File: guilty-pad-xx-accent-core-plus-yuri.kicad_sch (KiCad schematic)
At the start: 279 parts, among them J1 Conn_01x04_Socket, Q1 DMC3071LVT, SW1 SW_Push, SW10 SW_Push, SW11 SW_Push, SW12 SW_Push, SW13 SW_Push, SW14 SW_Push, SW15 SW_Push, SW16 SW_Push, SW17 SW_Push, SW18 SW_Push, SW19 SW_Push, SW2 SW_Push, SW20 SW_Push, SW21 SW_Push, SW22 SW_Push, SW23 SW_Push, SW24 SW_Push, SW25 SW_Push, SW26 SW_Push, SW27 SW_Push, SW28 SW_Push, SW29 SW_Push, SW3 SW_Push, SW30 SW_Push, SW31 SW_Push, SW32 SW_Push, SW33 SW_Push, SW34 SW_Push, SW35 SW_Push, SW36 SW_Push, SW37 SW_Push, SW38 SW_Push, SW39 SW_Push, SW4 SW_Push, SW40 SW_Push, SW41 SW_Push, SW42 SW_Push, SW43 SW_Push, SW44 SW_Push, SW45 SW_Push, SW46 SW_Push, SW47 SW_Push, SW48 SW_Push, SW49 SW_Push, SW5 SW_Push, SW50 SW_Push, SW51 SW_Push, SW52 SW_Push, SW53 SW_Push, SW54 SW_Push, SW55 SW_Push, SW56 SW_Push, SW57 SW_Push, SW58 SW_Push, SW59 SW_Push, SW6 SW_Push, SW60 SW_Push, SW61 SW_Push, SW62 SW_Push, SW63 SW_Push, SW64 SW_Push, SW65 SW_Push, SW66 SW_Push, SW67 SW_Push, SW68 SW_Push, SW69 SW_Push, SW7 SW_Push, SW70 SW_Push, SW71 SW_Push, SW72 SW_Push, SW73 SW_Push, SW74 SW_Push, SW75 SW_Push, SW76 SW_Push, SW77 SW_Push, SW78 SW_Push, SW79 SW_Push, SW8 SW_Push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

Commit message: schematic and pcb are done, images for those are added
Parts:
- removed LED88, LED89: MX_SK6803MINI-E, PCM_marbastlib-mx:LED_MX_6028R, symbol ggxxacpy:MX_SK6803MINI-E
- removed Q1: DMC3071LVT, Package_TO_SOT_SMD:TSOT-23-6_HandSoldering, symbol Transistor_FET:DMC3071LVT
- added Q1: G1NP02ELL, Package_TO_SOT_SMD:TSOT-23-6_HandSoldering, symbol ggxxacpy:G1NP02ELL
- added SW88: RotaryEncoder_Switch, Rotary_Encoder:RotaryEncoder_Alps_EC11E-Switch_Vertical_H20mm, symbol Device:RotaryEncoder_Switch
- D1, D10, D11, D12, D13, D14, D15, D16, D17, D18, D19, D2, D20, D21, D22, D23, D24, D25, D26, D27, D28, D29, D3, D30, D31, D32, D33, D34, D35, D36, D37, D38, D39, D4, D40, D41, D42, D43, D44, D45, D46, D47, D48, D49, D5, D50, D51, D52, D53, D54, D55, D56, D57, D58, D59, D6, D60, D61, D62, D63, D64, D65, D66, D67, D68, D69, D7, D70, D71, D72, D73, D74, D75, D76, D77, D78, D79, D8, D80, D81, D82, D83, D84, D85, D86, D87, D88, D9: footprint (none) -> Diode_SMD:D_SMA_Handsoldering
- D89: footprint Diode_SMD:D_SOD-123 -> Diode_SMD:D_SMA_Handsoldering
- J1: footprint (none) -> KiCad-SSD1306-0.91-OLED-4pin-128x32:SSD1306-0.91-OLED-4pin-128x32
- LED1, LED10, LED11, LED12, LED13, LED14, LED15, LED16, LED17, LED18, LED19, LED2, LED20, LED21, LED22, LED23, LED24, LED25, LED26, LED27, LED28, LED29, LED3, LED30, LED31, LED32, LED33, LED34, LED35, LED36, LED37, LED38, LED39, LED4, LED40, LED41, LED42, LED43, LED44, LED45, LED46, LED47, LED48, LED49, LED5, LED50, LED51, LED52, LED53, LED54, LED55, LED56, LED57, LED58, LED59, LED6, LED60, LED61, LED62, LED63, LED64, LED65, LED66, LED67, LED68, LED69, LED7, LED70, LED71, LED72, LED73, LED74, LED75, LED76, LED77, LED78, LED79, LED8, LED80, LED81, LED82, LED83, LED84, LED85, LED86, LED87, LED9: footprint PCM_marbastlib-mx:LED_MX_6028R -> gpxxacpy:LED_6028R
- R3, R4: footprint (none) -> Capacitor_SMD:C_0402_1005Metric_Pad0.74x0.62mm_HandSolder
- SW1, SW10, SW11, SW12, SW13, SW14, SW15, SW16, SW17, SW18, SW19, SW2, SW20, SW21, SW22, SW23, SW24, SW25, SW26, SW27, SW28, SW3, SW30, SW31, SW32, SW33, SW35, SW36, SW37, SW38, SW39, SW4, SW40, SW41, SW42, SW43, SW44, SW45, SW46, SW48, SW49, SW5, SW50, SW52, SW53, SW54, SW55, SW56, SW57, SW58, SW59, SW6, SW60, SW61, SW62, SW65, SW66, SW67, SW68, SW69, SW7, SW70, SW71, SW72, SW73, SW74, SW76, SW8, SW85, SW86, SW87, SW9: footprint (none) -> gpxxacpy:SW_Cherry_MX_1.00u_PCB
- SW29: footprint (none) -> gpxxacpy:SW_Cherry_MX_2.00u_PCB
- SW34, SW47: footprint (none) -> gpxxacpy:SW_Cherry_MX_1.50u_PCB
- SW51: footprint (none) -> gpxxacpy:SW_Cherry_MX_1.75u_PCB
- SW63, SW64: footprint (none) -> gpxxacpy:SW_Cherry_MX_2.25u_PCB
- SW75: footprint (none) -> gpxxacpy:SW_Cherry_MX_2.75u_PCB
- SW77, SW78, SW79, SW81, SW82, SW83, SW84: footprint (none) -> gpxxacpy:SW_Cherry_MX_1.25u_PCB
- SW80: footprint (none) -> gpxxacpy:SW_Cherry_MX_6.25u_PCB
- U1: footprint (none) -> OPL:XIAO-nRF52840-SMD
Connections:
- net +5V_USB: now also Q1.1 (G)
- net COL1: now also SW73.1, SW74.1, SW75.1, SW76.1, SW77.1, SW78.1, SW79.1, SW80.1, SW81.1
- net GND: now also Q1.5 (S), SW88.C, SW88.S2; no longer LED1.4 (VSS), LED10.4 (VSS), LED11.4 (VSS), LED12.4 (VSS), LED13.4 (VSS), LED14.4 (VSS), LED15.4 (VSS), LED16.4 (VSS), LED17.4 (VSS), LED18.4 (VSS), LED19.4 (VSS), LED2.4 (VSS), LED20.4 (VSS), LED21.4 (VSS), LED22.4 (VSS), LED23.4 (VSS), LED24.4 (VSS), LED25.4 (VSS), LED26.4 (VSS), LED27.4 (VSS), LED28.4 (VSS), LED29.4 (VSS), LED3.4 (VSS), LED30.4 (VSS), LED31.4 (VSS), LED32.4 (VSS), LED33.4 (VSS), LED34.4 (VSS), LED35.4 (VSS), LED36.4 (VSS), LED37.4 (VSS), LED38.4 (VSS), LED39.4 (VSS), LED4.4 (VSS), LED40.4 (VSS), LED41.4 (VSS), LED42.4 (VSS), LED43.4 (VSS), LED44.4 (VSS), LED45.4 (VSS), LED46.4 (VSS), LED47.4 (VSS), LED48.4 (VSS), LED49.4 (VSS), LED5.4 (VSS), LED50.4 (VSS), LED51.4 (VSS), LED52.4 (VSS), LED53.4 (VSS), LED54.4 (VSS), LED55.4 (VSS), LED56.4 (VSS), LED57.4 (VSS), LED58.4 (VSS), LED59.4 (VSS), LED6.4 (VSS), LED60.4 (VSS), LED61.4 (VSS), LED62.4 (VSS), LED63.4 (VSS), LED64.4 (VSS), LED65.4 (VSS), LED66.4 (VSS), LED67.4 (VSS), LED68.4 (VSS), LED69.4 (VSS), LED7.4 (VSS), LED70.4 (VSS), LED71.4 (VSS), LED72.4 (VSS), LED73.4 (VSS), LED74.4 (VSS), LED75.4 (VSS), LED76.4 (VSS), LED77.4 (VSS), LED78.4 (VSS), LED79.4 (VSS), LED8.4 (VSS), LED80.4 (VSS), LED81.4 (VSS), LED82.4 (VSS), LED83.4 (VSS), LED84.4 (VSS), LED85.4 (VSS), LED86.4 (VSS), LED87.4 (VSS), LED9.4 (VSS)
- net LED_ENABLE: now also Q1.3 (G)
- net LED_GND: now also LED1.4 (VSS), LED10.4 (VSS), LED11.4 (VSS), LED12.4 (VSS), LED13.4 (VSS), LED14.4 (VSS), LED15.4 (VSS), LED16.4 (VSS), LED17.4 (VSS), LED18.4 (VSS), LED19.4 (VSS), LED2.4 (VSS), LED20.4 (VSS), LED21.4 (VSS), LED22.4 (VSS), LED23.4 (VSS), LED24.4 (VSS), LED25.4 (VSS), LED26.4 (VSS), LED27.4 (VSS), LED28.4 (VSS), LED29.4 (VSS), LED3.4 (VSS), LED30.4 (VSS), LED31.4 (VSS), LED32.4 (VSS), LED33.4 (VSS), LED34.4 (VSS), LED35.4 (VSS), LED36.4 (VSS), LED37.4 (VSS), LED38.4 (VSS), LED39.4 (VSS), LED4.4 (VSS), LED40.4 (VSS), LED41.4 (VSS), LED42.4 (VSS), LED43.4 (VSS), LED44.4 (VSS), LED45.4 (VSS), LED46.4 (VSS), LED47.4 (VSS), LED48.4 (VSS), LED49.4 (VSS), LED5.4 (VSS), LED50.4 (VSS), LED51.4 (VSS), LED52.4 (VSS), LED53.4 (VSS), LED54.4 (VSS), LED55.4 (VSS), LED56.4 (VSS), LED57.4 (VSS), LED58.4 (VSS), LED59.4 (VSS), LED6.4 (VSS), LED60.4 (VSS), LED61.4 (VSS), LED62.4 (VSS), LED63.4 (VSS), LED64.4 (VSS), LED65.4 (VSS), LED66.4 (VSS), LED67.4 (VSS), LED68.4 (VSS), LED69.4 (VSS), LED7.4 (VSS), LED70.4 (VSS), LED71.4 (VSS), LED72.4 (VSS), LED73.4 (VSS), LED74.4 (VSS), LED75.4 (VSS), LED76.4 (VSS), LED77.4 (VSS), LED78.4 (VSS), LED79.4 (VSS), LED8.4 (VSS), LED80.4 (VSS), LED81.4 (VSS), LED82.4 (VSS), LED83.4 (VSS), LED84.4 (VSS), LED85.4 (VSS), LED86.4 (VSS), LED87.4 (VSS), LED9.4 (VSS), Q1.2 (S), Q1.4 (D)
- net ROW0: now also D18.1 (K), D35.1 (K), D52.1 (K), D78.1 (K); no longer D11.1 (K), D29.1 (K), D47.1 (K), D74.1 (K), D83.1 (K)
- net ROW1: now also D19.1 (K), D36.1 (K), D53.1 (K), D79.1 (K); no longer D12.1 (K), D30.1 (K), D48.1 (K), D75.1 (K), D84.1 (K)
- net ROW2: now also D17.1 (K), D29.1 (K), D45.1 (K), D48.1 (K), D62.1 (K), D73.1 (K), D74.1 (K), D84.1 (K); no longer D13.1 (K), D31.1 (K), D40.1 (K), D49.1 (K), D58.1 (K), D67.1 (K), D76.1 (K), D85.1 (K)
- net ROW3: now also D16.1 (K), D31.1 (K), D46.1 (K), D47.1 (K), D63.1 (K), D72.1 (K), D75.1 (K), D85.1 (K); no longer D14.1 (K), D32.1 (K), D41.1 (K), D50.1 (K), D59.1 (K), D68.1 (K), D77.1 (K), D86.1 (K)
- net ROW4: now also D30.1 (K), D44.1 (K), D54.1 (K), D64.1 (K), D67.1 (K), D77.1 (K), D88.1 (K); no longer D33.1 (K), D42.1 (K), D51.1 (K), D60.1 (K), D69.1 (K), D78.1 (K), D87.1 (K)
- net ROW5: now also D14.1 (K), D42.1 (K), D51.1 (K), D58.1 (K), D68.1 (K), D80.1 (K), D87.1 (K); no longer D16.1 (K), D43.1 (K), D52.1 (K), D61.1 (K), D70.1 (K), D79.1 (K), D88.1 (K)
- net ROW6: now also D13.1 (K), D33.1 (K), D43.1 (K), D50.1 (K), D59.1 (K), D69.1 (K), D81.1 (K), D86.1 (K); no longer D17.1 (K), D35.1 (K), D44.1 (K), D53.1 (K), D62.1 (K), D71.1 (K), D80.1 (K)
- net ROW7: now also D12.1 (K), D32.1 (K), D40.1 (K), D49.1 (K), D60.1 (K), D70.1 (K), D82.1 (K), D83.1 (K); no longer D18.1 (K), D36.1 (K), D45.1 (K), D54.1 (K), D63.1 (K), D72.1 (K), D81.1 (K)
- net ROW8: now also D11.1 (K), D41.1 (K), D61.1 (K), D71.1 (K), D76.1 (K); no longer D19.1 (K), D46.1 (K), D64.1 (K), D73.1 (K), D82.1 (K)
- net EC11_SW: now reaches U1.2 (P0.03_A1_D1)
- net EC11_SW: now also SW88.S1
- net EC11_B: now reaches U1.3 (P0.28_A2_D2)
- net EC11_B: now also SW88.B
- net EC11_A: now reaches U1.4 (P0.29_A3_D3)
- net EC11_A: now also SW88.A
- net at U3.2 (GND): now also Q1.6 (D)
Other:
- note added: "EC11 Rotary Encoder w/ Switch"
- note removed: "TODO: add rotary encoder!!!"
- moved on the sheet: C2, D10, D11, D12, D13, D14, D15, D16, D17, D18, D19, D2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

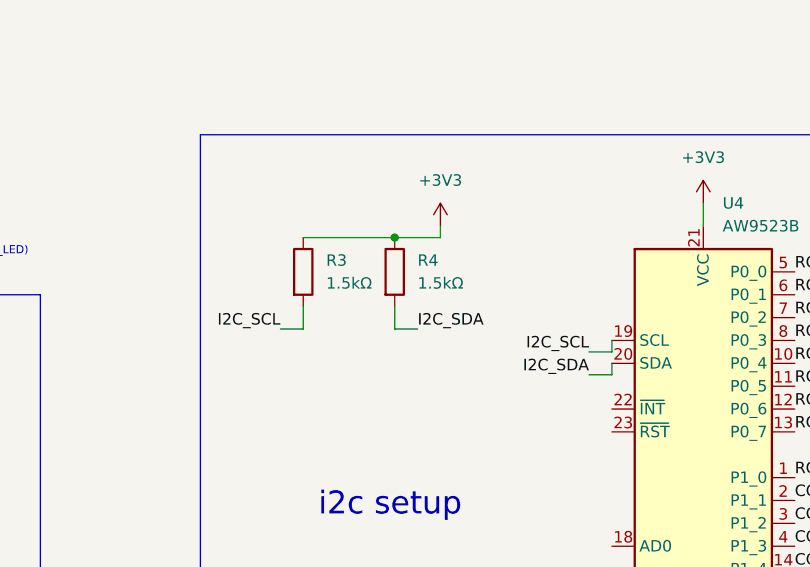
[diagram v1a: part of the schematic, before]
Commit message: update README/BOM, use 4.7k resistors for i2c pullup
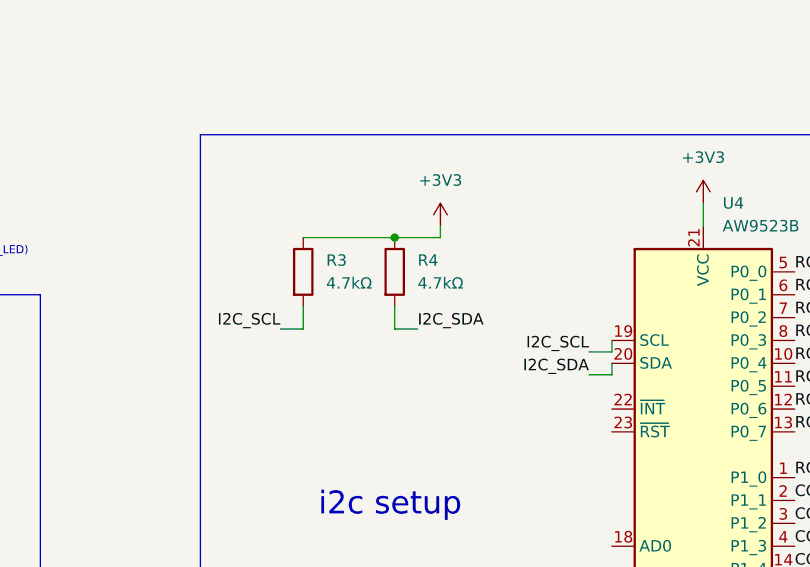
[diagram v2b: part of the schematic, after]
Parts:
- R3, R4: value 1.5kΩ -> 4.7kΩ
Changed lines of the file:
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@@
 			)
 		)
-		(property "Value" "1.5kΩ"
+		(property "Value" "4.7kΩ"
 			(at 130.81 223.5199 0)
 			(effects
@@
 			)
 		)
-		(property "Value" "1.5kΩ"
+		(property "Value" "4.7kΩ"
 			(at 120.65 223.5199 0)
 			(effects

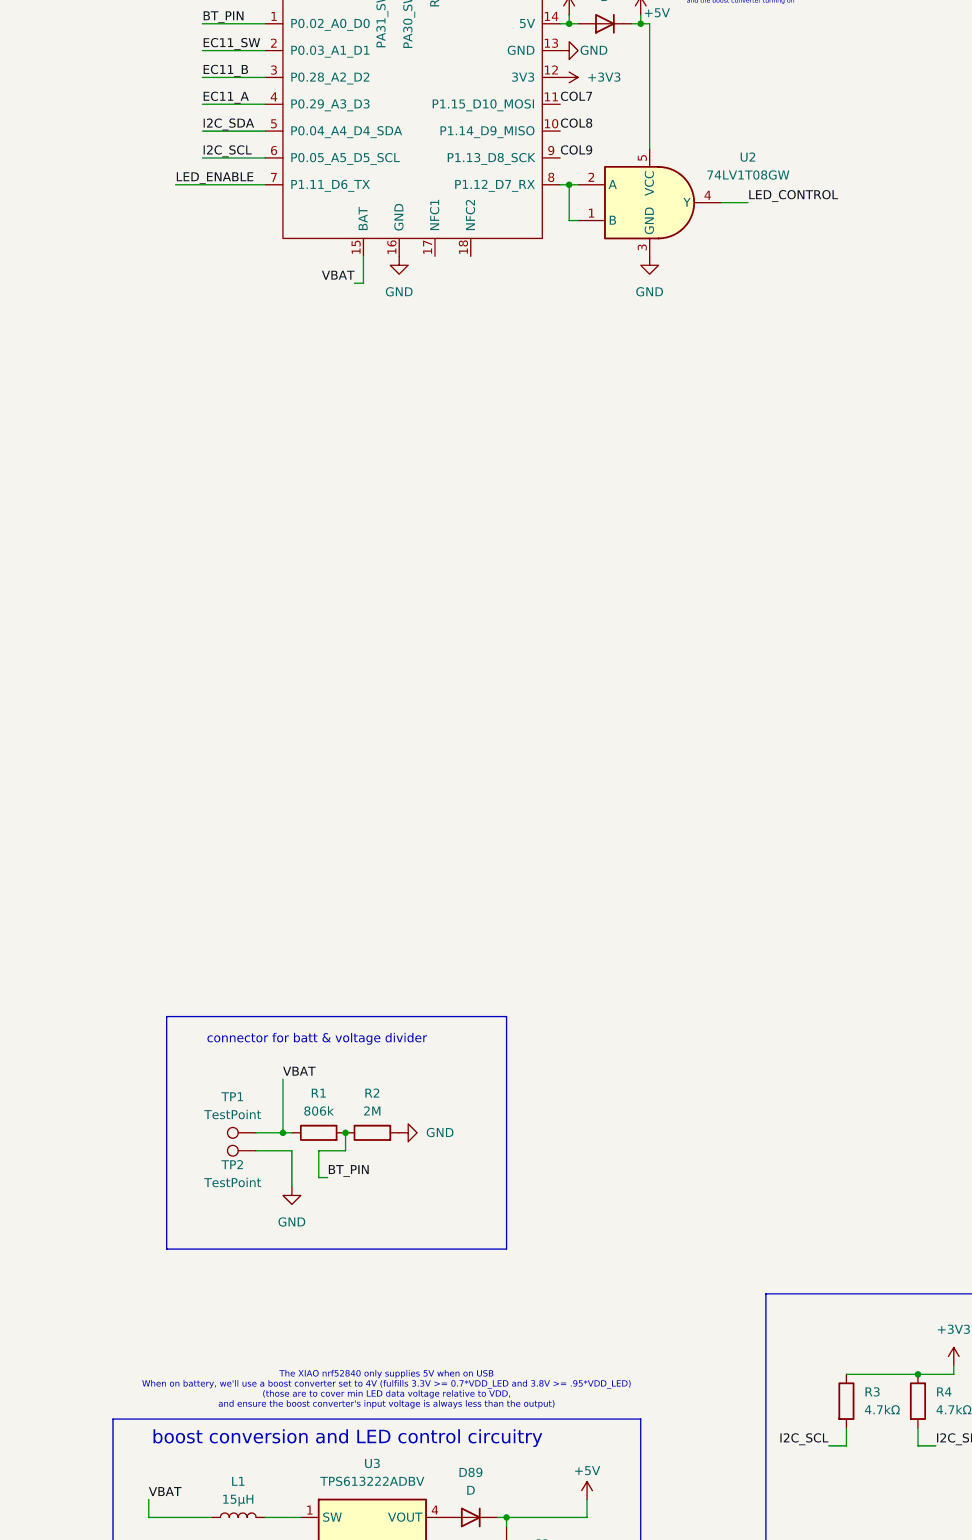
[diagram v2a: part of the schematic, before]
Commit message: no real schematic changes, just fix an old comment
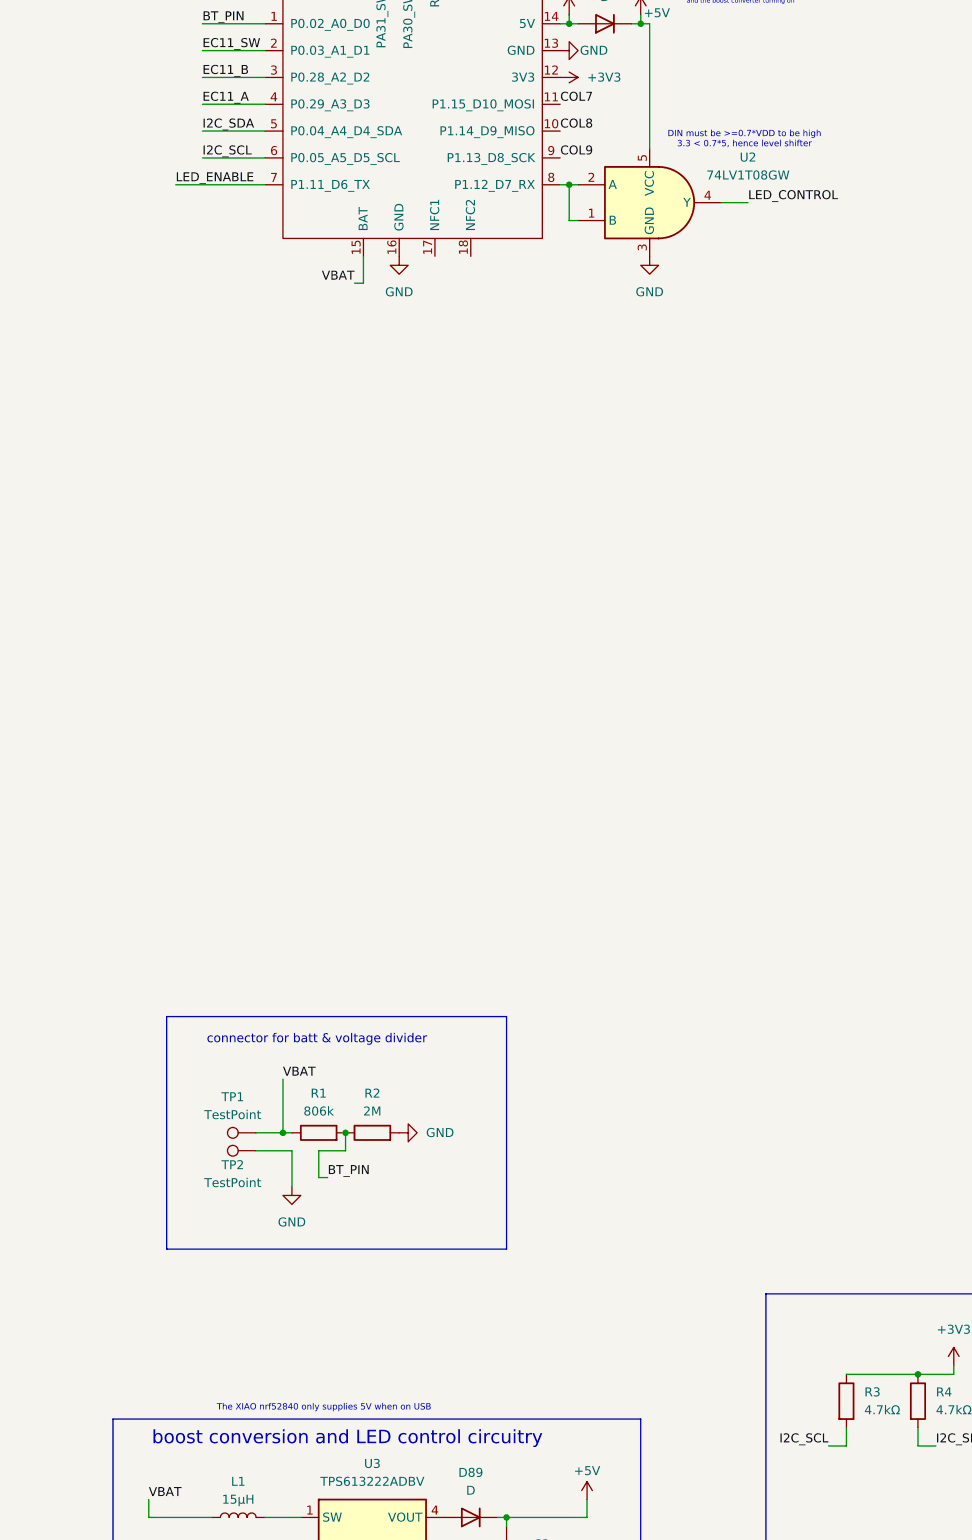
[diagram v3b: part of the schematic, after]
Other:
- note added: "DIN must be >=0.7*VDD to be high 3.3 < 0.7*5, hence level shifter"
- note added: "The XIAO nrf52840 only supplies 5V when on USB"
- note removed: "The XIAO nrf52840 only supplies 5V when on USB When on battery, we'll use a boost converter set to 4V (fulfills 3.3V >= 0.7*VDD_LED and 3.8V >= .95*VDD_LED) (those are to cover min LED data voltage relative to VDD, and ensure the boost converter's input voltage is always less than the output)"
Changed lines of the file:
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@@
 		)
 	)
-	(text "The XIAO nrf52840 only supplies 5V when on USB\nWhen on battery, we'll use a boost converter set to 4V (fulfills 3.3V >= 0.7*VDD_LED and 3.8V >= .95*VDD_LED)\n(those are to cover min LED data voltage relative to VDD,\nand ensure the boost converter's input voltage is always less than the output)"
+	(text "The XIAO nrf52840 only supplies 5V when on USB"
 		(exclude_from_sim no)
-		(at 52.832 220.726 0)
+		(at 43.942 223.266 0)
 		(effects
 			(font
@@
 			)
 		)
+	)
+	(text "DIN must be >=0.7*VDD to be high\n3.3 < 0.7*5, hence level shifter"
+		(exclude_from_sim no)
+		(at 103.632 43.18 0)
+		(effects
+			(font
+				(size 0.889 0.889)
+			)
+		)
